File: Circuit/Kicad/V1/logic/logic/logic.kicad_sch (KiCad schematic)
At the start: 6 parts

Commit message: LogicのPCBを途中まで作った
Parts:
- R_PU1, R_PU2: footprint (none) -> Resistor_THT:R_Axial_DIN0207_L6.3mm_D2.5mm_P10.16mm_Horizontal
- for_PG1: renamed from for_PG; footprint (none) -> DCDC_Converter:M78A
- to_RPI1: renamed from to_RPI5; footprint (none) -> DCDC_Converter:AE-MYMGK00506ERSR-5V0
- to_STM1: renamed from to_STM32; footprint (none) -> DCDC_Converter:AE-MYMGK00506ERSR-5V0
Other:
- removed sheet logic_p3

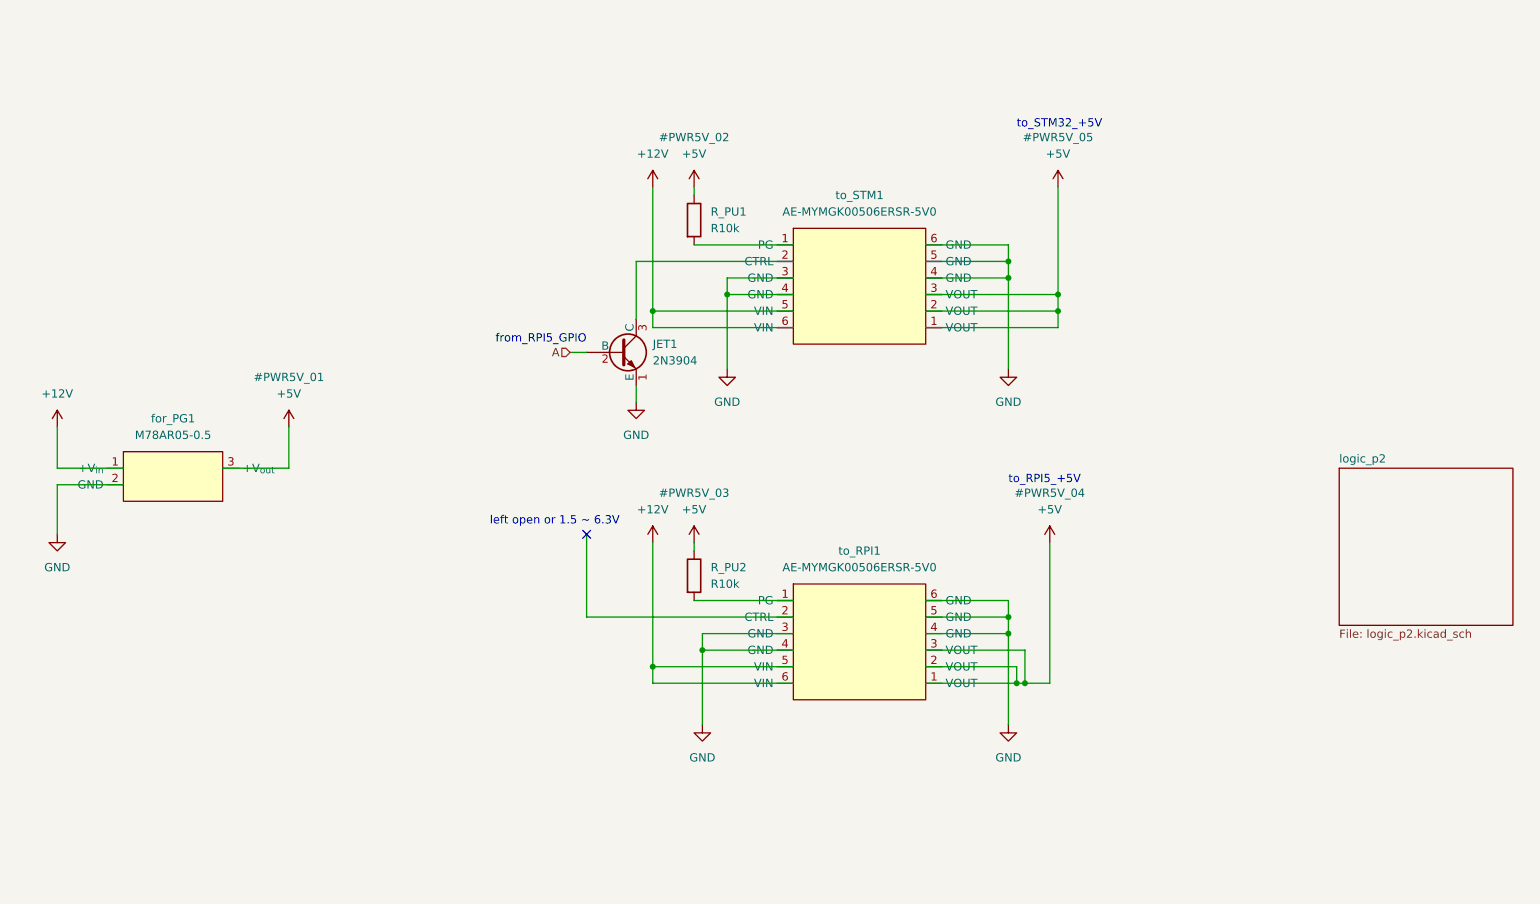
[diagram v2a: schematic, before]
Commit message: スイッチの追加と整理。
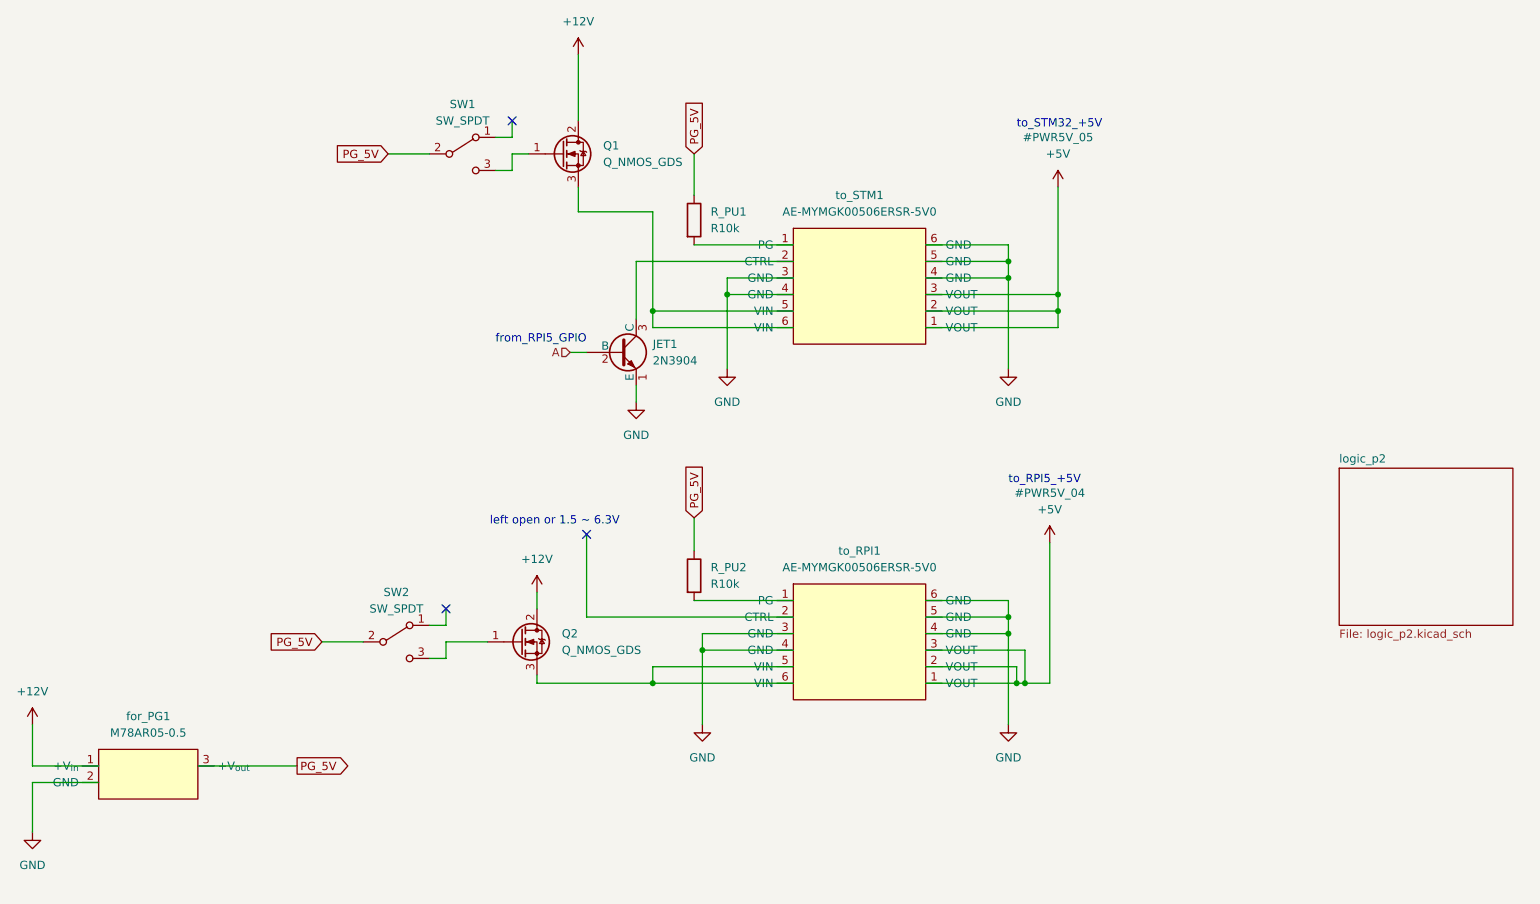
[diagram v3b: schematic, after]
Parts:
- added Q1, Q2: Q_NMOS_GDS, DCDC_Converter:EKI04036, symbol Device:Q_NMOS_GDS
- added SW1, SW2: SW_SPDT, DCDC_Converter:2MS1-T1-B4-VS2-Q-E-S, symbol Switch:SW_SPDT
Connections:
- net +12V: now also Q1.2 (D), Q2.2 (D); no longer to_RPI1.5 (VIN), to_RPI1.6 (VIN), to_STM1.5 (VIN), to_STM1.6 (VIN)
- net +5V: no longer R_PU1.1, R_PU2.1, for_PG1.3 (+V_{out})
- new net: Q2.3 (S), to_RPI1.5 (VIN), to_RPI1.6 (VIN)
- new net: Q1.1 (G), SW1.3 (C)
- new net: Q1.3 (S), to_STM1.5 (VIN), to_STM1.6 (VIN)
- new net: Q2.1 (G), SW2.3 (C)
- new net PG_5V: R_PU1.1, R_PU2.1, SW1.2 (B), SW2.2 (B), for_PG1.3 (+V_{out})
- no-connect marks 1 -> 3
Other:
- moved on the sheet: for_PG1

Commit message: Version1のLogic基板が、形はできた。検査や見積もりはまだ
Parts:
- added D_LED1, D_LED2: LED_red_withR, symbol Device:LED
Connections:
- net +5V: now also D_LED1.2 (A), D_LED2.2 (A)
- net GND: now also D_LED1.1 (K), D_LED2.1 (K)
- new net: Q2.3 (S), to_RPI1.5 (VIN), to_RPI1.6 (VIN)
- new net: Q1.3 (S), to_STM1.5 (VIN), to_STM1.6 (VIN)
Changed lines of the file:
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@@
   (junction (at 203.2 71.12) (diameter 0) (color 0 0 0 0)
   )
+  (junction (at 201.93 125.73) (diameter 0) (color 0 0 0 0)
+  )
+  (junction (at 201.93 130.81) (diameter 0) (color 0 0 0 0)
+  )
   (junction (at 195.58 66.04) (diameter 0) (color 0 0 0 0)
   )
+  (junction (at 201.93 128.27) (diameter 0) (color 0 0 0 0)
+  )
   (junction (at 140.97 73.66) (diameter 0) (color 0 0 0 0)
   )
@@
   (junction (at 148.59 125.73) (diameter 0) (color 0 0 0 0)
   )
-  (junction (at 196.85 130.81) (diameter 0) (color 0 0 0 0)
-  )
   (junction (at 203.2 73.66) (diameter 0) (color 0 0 0 0)
   )
-  (junction (at 198.12 130.81) (diameter 0) (color 0 0 0 0)
-  )
   (junction (at 195.58 68.58) (diameter 0) (color 0 0 0 0)
   )
   (junction (at 195.58 120.65) (diameter 0) (color 0 0 0 0)
+  )
+  (junction (at 203.2 76.2) (diameter 0) (color 0 0 0 0)
+  )
+  (junction (at 203.2 78.74) (diameter 0) (color 0 0 0 0)
   )
   (no_connect (at 119.38 44.45))
   (no_connect (at 130.81 107.95))
   (no_connect (at 109.22 119.38))
-  (wire (pts (xy 196.85 130.81) (xy 198.12 130.81))
-    (stroke (width 0) (type default) (color 0 0 0 0))
-  )
   (wire (pts (xy 182.88 76.2) (xy 203.2 76.2))
     (stroke (width 0) (type default) (color 0 0 0 0))
@@
     (stroke (width 0) (type default) (color 0 0 0 0))
   )
-  (wire (pts (xy 196.85 128.27) (xy 196.85 130.81))
-    (stroke (width 0) (type default) (color 0 0 0 0))
-  )
   (wire (pts (xy 162.56 128.27) (xy 140.97 128.27))
     (stroke (width 0) (type default) (color 0 0 0 0))
@@
     (stroke (width 0) (type default) (color 0 0 0 0))
   )
-  (wire (pts (xy 182.88 125.73) (xy 198.12 125.73))
+  (wire (pts (xy 182.88 125.73) (xy 201.93 125.73))
     (stroke (width 0) (type default) (color 0 0 0 0))
   )
@@
     (stroke (width 0) (type default) (color 0 0 0 0))
   )
+  (wire (pts (xy 201.93 140.97) (xy 201.93 144.78))
+    (stroke (width 0) (type default) (color 0 0 0 0))
+  )
   (wire (pts (xy 109.22 127) (xy 106.68 127))
     (stroke (width 0) (type default) (color 0 0 0 0))
@@
     (stroke (width 0) (type default) (color 0 0 0 0))
   )
-  (wire (pts (xy 182.88 128.27) (xy 196.85 128.27))
+  (wire (pts (xy 182.88 128.27) (xy 201.93 128.27))
+    (stroke (width 0) (type default) (color 0 0 0 0))
+  )
+  (wire (pts (xy 201.93 130.81) (xy 201.93 133.35))
     (stroke (width 0) (type default) (color 0 0 0 0))
   )
@@
     (stroke (width 0) (type default) (color 0 0 0 0))
   )
-  (wire (pts (xy 198.12 130.81) (xy 201.93 130.81))
-    (stroke (width 0) (type default) (color 0 0 0 0))
-  )
   (wire (pts (xy 195.58 66.04) (xy 195.58 68.58))
     (stroke (width 0) (type default) (color 0 0 0 0))
@@
     (stroke (width 0) (type default) (color 0 0 0 0))
   )
+  (wire (pts (xy 203.2 86.36) (xy 203.2 88.9))
+    (stroke (width 0) (type default) (color 0 0 0 0))
+  )
   (wire (pts (xy 148.59 125.73) (xy 148.59 137.16))
     (stroke (width 0) (type default) (color 0 0 0 0))
   )
-  (wire (pts (xy 201.93 109.22) (xy 201.93 130.81))
+  (wire (pts (xy 201.93 109.22) (xy 201.93 125.73))
     (stroke (width 0) (type default) (color 0 0 0 0))
   )
@@
     (stroke (width 0) (type default) (color 0 0 0 0))
   )
+  (wire (pts (xy 203.2 76.2) (xy 203.2 78.74))
+    (stroke (width 0) (type default) (color 0 0 0 0))
+  )
   (wire (pts (xy 90.17 124.46) (xy 96.52 124.46))
     (stroke (width 0) (type default) (color 0 0 0 0))
   )
+  (wire (pts (xy 201.93 128.27) (xy 201.93 130.81))
+    (stroke (width 0) (type default) (color 0 0 0 0))
+  )
   (wire (pts (xy 45.72 143.51) (xy 45.72 137.16))
     (stroke (width 0) (type default) (color 0 0 0 0))
@@
     (stroke (width 0) (type default) (color 0 0 0 0))
   )
+  (wire (pts (xy 182.88 130.81) (xy 201.93 130.81))
+    (stroke (width 0) (type default) (color 0 0 0 0))
+  )
   (wire (pts (xy 138.43 85.09) (xy 138.43 87.63))
     (stroke (width 0) (type default) (color 0 0 0 0))
@@
     (stroke (width 0) (type default) (color 0 0 0 0))
   )
-  (wire (pts (xy 198.12 125.73) (xy 198.12 130.81))
+  (wire (pts (xy 201.93 125.73) (xy 201.93 128.27))
     (stroke (width 0) (type default) (color 0 0 0 0))
   )
@@
     (stroke (width 0) (type default) (color 0 0 0 0))
   )
+  (wire (pts (xy 203.2 78.74) (xy 203.2 80.01))
+    (stroke (width 0) (type default) (color 0 0 0 0))
+  )
   (wire (pts (xy 152.4 71.12) (xy 162.56 71.12))
     (stroke (width 0) (type default) (color 0 0 0 0))
@@
   )
   (wire (pts (xy 100.33 49.53) (xy 106.68 49.53))
-    (stroke (width 0) (type default) (color 0 0 0 0))
-  )
-  (wire (pts (xy 182.88 130.81) (xy 196.85 130.81))
     (stroke (width 0) (type default) (color 0 0 0 0))
   )
@@
     (pin "6")
   )
+  (symbol (lib_id "Device:LED") (at 203.2 82.55 90) (unit 1)
+    (in_bom yes) (on_board yes) (fields_autoplaced)
+    (property "Reference" "D_LED2" (id 0) (at 207.01 82.8674 90)
+      (effects (font (size 1.27 1.27)) (justify right))
+    )
+    (property "Value" "LED_red_withR" (id 1) (at 207.01 85.4074 90)
+      (effects (font (size 1.27 1.27)) (justify right))
+    )
+    (property "Footprint" "" (id 2) (at 203.2 82.55 0)
+      (effects (font (size 1.27 1.27)) hide)
+    )
+    (property "Datasheet" "~" (id 3) (at 203.2 82.55 0)
+      (effects (font (size 1.27 1.27)) hide)
+    )
+    (pin "1")
+    (pin "2")
+  )
   (symbol (lib_id "DCDC_Converter:M78AR05-0.5") (at 63.5 146.05 0) (unit 1)
     (in_bom yes) (on_board yes) (fields_autoplaced)
@@
     (pin "2")
     (pin "3")
+  )
+  (symbol (lib_id "Device:LED") (at 201.93 137.16 90) (unit 1)
+    (in_bom yes) (on_board yes) (fields_autoplaced)
+    (property "Reference" "D_LED1" (id 0) (at 205.74 137.4774 90)
+      (effects (font (size 1.27 1.27)) (justify right))
+    )
+    (property "Value" "LED_red_withR" (id 1) (at 205.74 140.0174 90)
+      (effects (font (size 1.27 1.27)) (justify right))
+    )
+    (property "Footprint" "" (id 2) (at 201.93 137.16 0)
+      (effects (font (size 1.27 1.27)) hide)
+    )
+    (property "Datasheet" "~" (id 3) (at 201.93 137.16 0)
+      (effects (font (size 1.27 1.27)) hide)
+    )
+    (pin "1")
+    (pin "2")
   )
   (symbol (lib_id "power:+12V") (at 129.54 34.29 0) (unit 1)
@@
     (pin "1")
   )
+  (symbol (lib_id "power:GND") (at 203.2 88.9 0) (unit 1)
+    (in_bom yes) (on_board yes) (fields_autoplaced)
+    (property "Reference" "#PWR?" (id 0) (at 203.2 95.25 0)
+      (effects (font (size 1.27 1.27)) hide)
+    )
+    (property "Value" "GND" (id 1) (at 203.2 93.98 0))
+    (property "Footprint" "" (id 2) (at 203.2 88.9 0)
+      (effects (font (size 1.27 1.27)) hide)
+    )
+    (property "Datasheet" "" (id 3) (at 203.2 88.9 0)
+      (effects (font (size 1.27 1.27)) hide)
+    )
+    (pin "1")
+  )
   (symbol (lib_id "power:GND") (at 148.59 137.16 0) (unit 1)
     (in_bom yes) (on_board yes) (fields_autoplaced)
@@
     (pin "1")
   )
+  (symbol (lib_id "power:GND") (at 201.93 144.78 0) (unit 1)
+    (in_bom yes) (on_board yes) (fields_autoplaced)
+    (property "Reference" "#PWR?" (id 0) (at 201.93 151.13 0)
+      (effects (font (size 1.27 1.27)) hide)
+    )
+    (property "Value" "GND" (id 1) (at 201.93 149.86 0))
+    (property "Footprint" "" (id 2) (at 201.93 144.78 0)
+      (effects (font (size 1.27 1.27)) hide)
+    )
+    (property "Datasheet" "" (id 3) (at 201.93 144.78 0)
+      (effects (font (size 1.27 1.27)) hide)
+    )
+    (pin "1")
+  )
   (sheet (at 246.38 97.79) (size 26.67 24.13) (fields_autoplaced)
     (stroke (width 0.1524) (type solid) (color 0 0 0 0))
@@
       (reference "#PWR?") (unit 1) (value "+12V") (footprint "")
     )
+    (path "/e24f23e8-cf8a-4d4d-8cd3-9b82b30de144"
+      (reference "#PWR?") (unit 1) (value "GND") (footprint "")
+    )
+    (path "/f75f9982-5008-48e2-bd31-759a0f8661d5"
+      (reference "#PWR?") (unit 1) (value "GND") (footprint "")
+    )
     (path "/c50f7880-ee13-443c-9844-68b08c672e4b/5d791cef-0aee-47d0-bfec-ee15c9e21027/16a8045b-c926-45e8-a6dc-0b6e29330cdd"
       (reference "C1_Bypass1") (unit 1) (value "C_0.1uF") (footprint "CAN_Pheripheral:GRM188F11H104ZA01")
@@
       (reference "D4") (unit 1) (value "LED_Red") (footprint "")
     )
+    (path "/2fc28578-a1a8-459c-ae97-83a0c087cc34"
+      (reference "D_LED1") (unit 1) (value "LED_red_withR") (footprint "")
+    )
+    (path "/02b8edd8-af00-4a29-859a-bb8148f5299c"
+      (reference "D_LED2") (unit 1) (value "LED_red_withR") (footprint "")
+    )
     (path "/c50f7880-ee13-443c-9844-68b08c672e4b/5d791cef-0aee-47d0-bfec-ee15c9e21027/6ad5adc9-794a-44b1-829c-443863c08d79"
       (reference "FB1") (unit 1) (value "FerriteBead") (footprint "CAN_Pheripheral:BLM21PG331SN")
@@
     )
     (path "/c50f7880-ee13-443c-9844-68b08c672e4b/5d791cef-0aee-47d0-bfec-ee15c9e21027/1a3c6315-fa11-44fc-91cd-d8ea964947c2"
-      (reference "R3") (unit 1) (value "R_120") (footprint "")
+      (reference "R3") (unit 1) (value "R_1k") (footprint "")
     )
     (path "/c50f7880-ee13-443c-9844-68b08c672e4b/5d791cef-0aee-47d0-bfec-ee15c9e21027/f1347c7e-7929-4153-ac3f-4fd7316dddd7"
-      (reference "R4") (unit 1) (value "R_120") (footprint "")
+      (reference "R4") (unit 1) (value "R_1k") (footprint "")
     )
     (path "/c50f7880-ee13-443c-9844-68b08c672e4b/5d791cef-0aee-47d0-bfec-ee15c9e21027/1a7cf58e-bf08-4d04-ab69-6cd9da0f441e"
@@
     )
     (path "/c50f7880-ee13-443c-9844-68b08c672e4b/5d791cef-0aee-47d0-bfec-ee15c9e21027/f145eed6-162d-45ab-b2ab-a0ed0bf7cf1f"
-      (reference "R7") (unit 1) (value "R_120") (footprint "")
+      (reference "R7") (unit 1) (value "R_1k") (footprint "")
     )
     (path "/c50f7880-ee13-443c-9844-68b08c672e4b/5d791cef-0aee-47d0-bfec-ee15c9e21027/78fe8b1c-9e8f-42c4-ae8a-b704c333d1ab"
-      (reference "R8") (unit 1) (value "R_120") (footprint "")
+      (reference "R8") (unit 1) (value "R_1k") (footprint "")
     )
     (path "/d601cad4-eff3-4bc2-a164-7532333b1c67"
